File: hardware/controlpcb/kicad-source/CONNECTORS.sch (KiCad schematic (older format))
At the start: 25 parts, among them CN1 691322310002, CN2 691322310004, CN3 691322310004, CN4 691322310004, CN5 691322310004, P6 CONN_01X08, P7 CONN_02X10, P8 CONN_01X03, Q4 2N7002

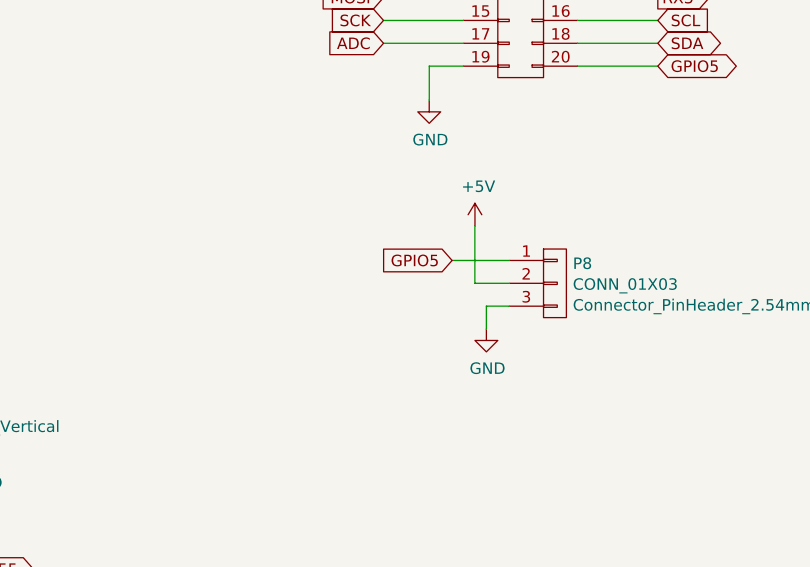
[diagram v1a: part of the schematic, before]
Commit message: added servo connector
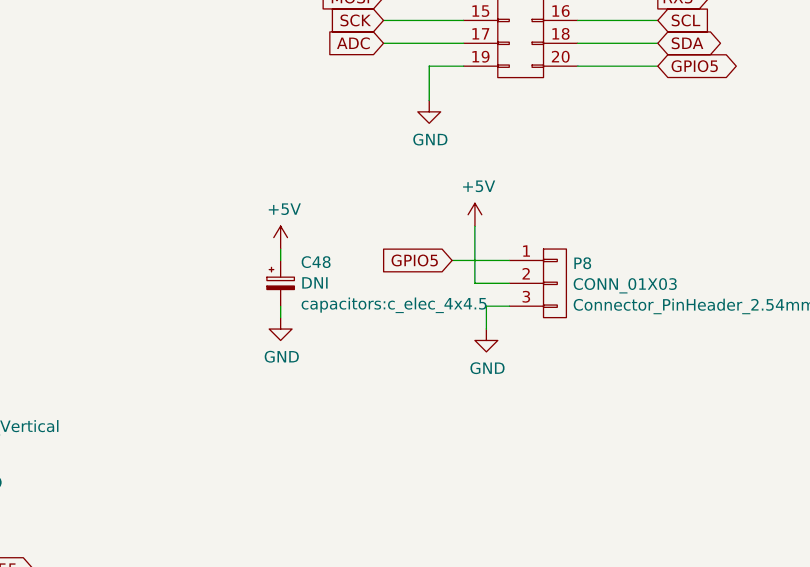
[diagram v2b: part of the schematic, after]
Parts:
- added C48: DNI, capacitors:c_elec_4x4.5, symbol devices:CP_Small
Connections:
- net +5V: now also C48.1
- net GND: now also C48.2
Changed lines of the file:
@@
 	1    0    0    -1
 $EndComp
+$Comp
+L devices:CP_Small C48
+U 1 1 5ED62ECA
+P 3950 5600
+F 0 "C48" H 4038 5691 50  0000 L CNN
+F 1 "DNI" H 4038 5600 50  0000 L CNN
+F 2 "capacitors:c_elec_4x4.5" H 4038 5509 50  0000 L CNN
+F 3 "" H 3950 5600 50  0000 C CNN
+	1    3950 5600
+	1    0    0    -1
+$EndComp
+$Comp
+L power-supply:+5V #PWR0117
+U 1 1 5ED63EE5
+P 3950 5450
+F 0 "#PWR0117" H 3950 5300 50  0001 C CNN
+F 1 "+5V" H 3965 5623 50  0000 C CNN
+F 2 "" H 3950 5450 50  0000 C CNN
+F 3 "" H 3950 5450 50  0000 C CNN
+	1    3950 5450
+	1    0    0    -1
+$EndComp
+$Comp
+L power-supply:GND #PWR0118
+U 1 1 5ED6445F
+P 3950 5750
+F 0 "#PWR0118" H 3950 5500 50  0001 C CNN
+F 1 "GND" H 3955 5577 50  0000 C CNN
+F 2 "" H 3950 5750 50  0000 C CNN
+F 3 "" H 3950 5750 50  0000 C CNN
+	1    3950 5750
+	1    0    0    -1
+$EndComp
+Wire Wire Line
+	3950 5500 3950 5450
+Wire Wire Line
+	3950 5750 3950 5700
 $EndSCHEMATC
